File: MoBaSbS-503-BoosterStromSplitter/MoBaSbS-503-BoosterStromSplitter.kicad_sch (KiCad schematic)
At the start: 5 parts, among them J1 39-28-1043, J2 39-28-1043, J3 39-28-1043, J4 39-28-1043, J5 39-28-1043

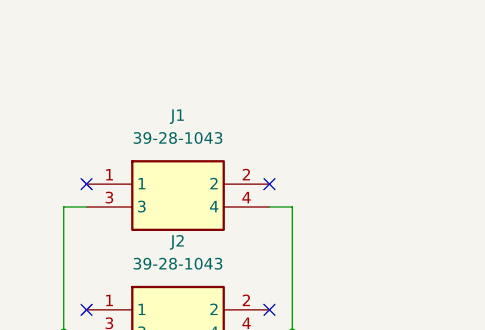
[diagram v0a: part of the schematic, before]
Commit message: Finished up PCBs, added stencil
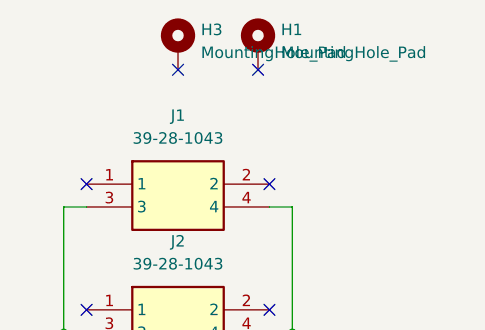
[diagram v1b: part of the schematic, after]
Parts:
- added H1, H3: MountingHole_Pad, MountingHole:MountingHole_2.7mm_M2.5_DIN965_Pad, symbol Mechanical:MountingHole_Pad
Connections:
- no-connect marks 10 -> 12
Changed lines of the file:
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@@
+	)
+	(no_connect
+		(at 93.98 54.61)
 	)
 	(no_connect
 		(at 104.14 95.25)
+	)
+	(no_connect
+		(at 102.87 54.61)
 	)
 	(no_connect
@@
 	)
 	(symbol
+		(lib_id "Mechanical:MountingHole_Pad")
+		(at 93.98 52.07 0)
+		(unit 1)
+		(exclude_from_sim no)
+		(in_bom yes)
+		(on_board yes)
+		(dnp no)
+		(fields_autoplaced yes)
+		(property "Reference" "H3"
+			(at 96.52 50.165 0)
+			(effects
+				(font
+					(size 1.27 1.27)
+				)
+				(justify left)
+			)
+		)
+		(property "Value" "MountingHole_Pad"
+			(at 96.52 52.705 0)
+			(effects
+				(font
+					(size 1.27 1.27)
+				)
+				(justify left)
+			)
+		)
+		(property "Footprint" "MountingHole:MountingHole_2.7mm_M2.5_DIN965_Pad"
+			(at 93.98 52.07 0)
+			(effects
+				(font
+					(size 1.27 1.27)
+				)
+				(hide yes)
+			)
+		)
+		(property "Datasheet" "~"
+			(at 93.98 52.07 0)
+			(effects
+				(font
+					(size 1.27 1.27)
+				)
+				(hide yes)
+			)
+		)
+		(property "Description" ""
+			(at 93.98 52.07 0)
+			(effects
+				(font
+					(size 1.27 1.27)
+				)
+				(hide yes)
+			)
+		)
+		(pin "1"
+		)
+		(instances
+			(project "MoBaSbS-503-BoosterStromSplitter"
+				(path "/ceabac13-b87f-4975-a621-d374a880bf70"
+					(reference "H3")
+					(unit 1)
+				)
+			)
+		)
+	)
+	(symbol
 		(lib_id "Molex_MiniFitJr_2x2_PCB:39-28-1043")
 		(at 83.82 81.28 0)
@@
 					(unit 1)
 				)
+			)
+		)
+	)
+	(symbol
+		(lib_id "Mechanical:MountingHole_Pad")
+		(at 102.87 52.07 0)
+		(unit 1)
+		(exclude_from_sim no)
+		(in_bom yes)
+		(on_board yes)
+		(dnp no)
+		(fields_autoplaced yes)
+		(property "Reference" "H1"
+			(at 105.41 50.165 0)
+			(effects
+				(font
+					(size 1.27 1.27)
+				)
+				(justify left)
+			)
+		)
+		(property "Value" "MountingHole_Pad"
+			(at 105.41 52.705 0)
+			(effects
+				(font
+					(size 1.27 1.27)
+				)
+				(justify left)
+			)
+		)
+		(property "Footprint" "MountingHole:MountingHole_2.7mm_M2.5_DIN965_Pad"
+			(at 102.87 52.07 0)
+			(effects
+				(font
+					(size 1.27 1.27)
+				)
+				(hide yes)
+			)
+		)
+		(property "Datasheet" "~"
+			(at 102.87 52.07 0)
+			(effects
+				(font
+					(size 1.27 1.27)
+				)
+				(hide yes)
+			)
+		)
+		(property "Description" ""
+			(at 102.87 52.07 0)
+			(effects
+				(font
+					(size 1.27 1.27)
+				)
+				(hide yes)
+			)
+		)
+		(pin "1"
+		)
+		(instances
+			(project "MoBaSbS-503-BoosterStromSplitter"
+				(path "/ceabac13-b87f-4975-a621-d374a880bf70"
+					(reference "H1")
+					(unit 1)
+				)
